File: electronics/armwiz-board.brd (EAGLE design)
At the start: 140.2 x 91.5 mm, 89 parts, among them J1 MICRO-SDCARD-CONNECTOR-330006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, J2 CORTEX_DEBUGSMD, U1 STM32F10XRXT6, U4 MIC5219-3.3V, X1 FH12-12S-1S, Y3 32.768kHz

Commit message: Really close now.
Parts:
- removed TP2, TP3, TP4: TPB1,27, testpad:B1,27
- added J15: Cortex Debug, SparkFun-Connectors:SAMTECH_FTSH-105-01
- added J16: ST-Link v2, SparkFun-Connectors:2X10
- added J17, J18: (no value), SparkFun-Connectors:1X01NS-KIT
- added R23: 100R, resistor:R0402
- added R24: 10K, resistor:R0402
- J14: device SparkFun-Connectors:1X25 -> PaxInstruments-Connectors:CONNECTORS_2X3_SMT_POSTS_T400
- moved J14 70.4 mm to (87.6, 33.0), flipped to the bottom, turned to 270 degrees
- moved R21 58.3 mm to (87.2, 4.50), turned to 270 degrees
- moved SJ2 37.9 mm to (85.0, 2.50), flipped to the bottom
- moved C18 37.2 mm to (83.2, 41.8), turned to 90 degrees
- moved R20 36.6 mm to (83.2, 37.2), turned to 90 degrees
- moved R4 32.4 mm to (82.0, 37.2)
- moved R2 32.0 mm to (84.5, 37.2)
- moved R18 29.8 mm to (85.8, 37.2), turned to 90 degrees
- moved C3 27.5 mm to (87.0, 34.0)
- moved R28 23.4 mm to (88.2, 34.0), turned to 270 degrees
- moved J2 20.9 mm to (87.2, 42.5), turned to 180 degrees
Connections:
- new net AD_GND: J15.3, J15.5, J15.9, J16.10, J16.12, J16.14, J16.16, J16.18, J16.20, J16.4, J16.6, J16.8
- new net AD_NRST: J15.10, J16.15
- new net AD_SWDCLK: J15.4, J16.9
- new net AD_SWDIO: J15.2, J16.7
- new net AD_SWO: J15.6, J16.13
- new net AD_TDI: J15.8, J16.5
- new net AD_VCC: J15.1, J16.1
- new net N$12: J2.6, R23.2
- net 3.3V: now also J14.1, J18.1, R24.2
- net BOOT0: now also J17.1; no longer TP2.TP
- net GND: now also J14.3; no longer J2.7
- net NRST: now also J14.5
- net SWDCLK: now also J14.2
- net SWDIO: now also J14.4
- net SWO: now also J14.6, R23.1, R24.1; no longer J2.6
- net USART1_RX: no longer TP3.TP
- net USART1_TX: no longer TP4.TP
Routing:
- net NRST: track 51.7 -> 104.7 mm, vias 1 -> 4
- net SWO: track 38.6 -> 91.6 mm, vias 0 -> 1
- net SW_A: track 54.6 -> 105.6 mm, vias 1 -> 2
- net SW_B: track 54.2 -> 91.2 mm, vias 1 -> 2
- net SWDIO: track 66.3 -> 99.2 mm, vias 1 -> 3
- net SWDCLK: track 63.0 -> 95.0 mm, vias 1 -> 3
- net RTC_BAT: track 47.2 -> 70.0 mm
- net SW_C: track 60.2 -> 83.0 mm, vias 1 -> 2
- net BOOT0: track 51.5 -> 74.0 mm, vias 1 -> 2
- net GND: track 81.1 -> 98.2 mm, vias 33 -> 41
- net BOOT1: track 55.3 -> 71.1 mm, vias 1 -> 3
- net 3.3V: track 47.8 -> 59.8 mm, vias 20 -> 28
- net N$13: track 0.00 -> 3.16 mm, vias 0 -> 1
- net N$12: track 0.00 -> 2.50 mm, vias 0 -> 1
- net N$5: track 0.00 -> 2.28 mm, vias 0 -> 1
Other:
- board size 140.2 x 91.5 mm -> 140.2 x 92.3 mm

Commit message: Four more wires.
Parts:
- added J22: (no value), SparkFun-Connectors:1X01
- moved J15 0.75 mm to (66.8, 35.5)
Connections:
- net PC1: now also J22.1
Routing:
- net AD_GND: track 0.00 -> 41.5 mm
- net AD_TDI: track 0.00 -> 13.5 mm, vias 0 -> 1
- net AD_VCC: track 0.00 -> 12.6 mm
- net AD_SWO: track 0.00 -> 7.11 mm
- net GND: track 98.2 -> 104.0 mm, vias 41 -> 44
- net AD_NRST: track 0.00 -> 5.65 mm
- net AD_SWDIO: track 0.00 -> 4.59 mm
- net AD_SWDCLK: track 0.00 -> 4.07 mm
- net N$14: track 0.00 -> 3.81 mm, vias 0 -> 1
- net SW_A: track 105.6 -> 102.8 mm
- net NRST: track 104.7 -> 102.5 mm
- net 3.3V: track 59.8 -> 61.3 mm
- net SW_B: track 91.2 -> 89.8 mm

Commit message: Added datasheets. This might be the final board layout and routing. Waiting on feedback.
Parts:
- removed J32, J9: (no value), SparkFun-Connectors:1X01
- removed R28: 10K, resistor:R0402
- added C12, C16, C17: 10uF, resistor:C0402K
- added C5, C7: 0.1uF, resistor:C0402K
- added J$1: SMA_EDGE, SparkFun-Connectors:SMA-EDGE
- added J23: (no value), SparkFun-Connectors:1X01
- added J25: (no value), PaxInstruments-Connectors:CONNECTORS_2X3_SMT_POSTS_T400
- added R25, R26: 10K, resistor:R0402
- moved J26 84.6 mm to (29.2, 43.2)
- moved J27 84.6 mm to (26.7, 43.2)
- moved U$6 74.5 mm to (73.3, 3.73), flipped to the bottom
- moved J21 5.08 mm to (55.9, 18.4)
- moved J20 2.54 mm to (50.8, 18.4)
- moved J11 2.54 mm to (40.6, 18.4)
- moved J22 2.54 mm to (48.3, 18.4)
- moved J24 2.54 mm to (38.1, 18.4)
- moved J33 2.54 mm to (45.7, 18.4)
- moved J7 2.54 mm to (43.2, 18.4)
- moved J8 2.54 mm to (53.3, 18.4)
- moved U$7 1.68 mm to (34.5, 12.8)
- moved C8 0.25 mm to (31.0, 14.2), turned to 180 degrees
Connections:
- removed net PB11: J9.1, U1.30
- removed net PC5: J32.1, U1.25
- new net N$14: J$1.GND@1, J$1.GND@3, J26.1
- new net N$15: J$1.GND@0, J$1.GND@2, J23.1
- new net N$16: R25.1, U$3.P$1
- new net N$20: J$1.SIG, J27.1
- new net VBAT2: R25.2, R26.1, U1.25
- net 3.3V: now also C12.2, C16.2, C17.2, C5.1, C7.1, J25.1; no longer R28.2
- net GND: now also C12.1, C16.1, C17.1, C5.2, C7.2, J25.5, R26.2
- net NRST: no longer R28.1
- net USART1_RX: now also J25.2; no longer J26.1
- net USART1_TX: now also J25.4; no longer J27.1
- net VBUS: now also U1.30
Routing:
- net VBAT2: track 0.00 -> 67.7 mm, vias 0 -> 2
- net PC5: track 46.8 -> 0.00 mm, vias 2 -> 0
- net SW_D: track 8.68 -> 42.7 mm, vias 0 -> 2
- net PB11: track 29.7 -> 0.00 mm, vias 2 -> 0
- net SW_E: track 7.76 -> 33.1 mm, vias 0 -> 2
- net USART1_RX: track 60.3 -> 46.8 mm
- net VBUS: track 25.4 -> 36.6 mm
- net 3.3V: track 61.3 -> 71.5 mm, vias 28 -> 30
- net N$15: track 0.00 -> 10.2 mm
- net N$16: track 0.00 -> 10.2 mm, vias 0 -> 1
- net USART1_TX: track 57.5 -> 48.9 mm, vias 1 -> 3
- net PC13: track 39.7 -> 33.0 mm
- net N$14: track 3.81 -> 10.2 mm, vias 1 -> 0
- net N$20: track 0.00 -> 5.08 mm
- net GND: track 104.0 -> 109.0 mm, vias 44 -> 50
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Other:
- board size 140.2 x 92.3 mm -> 99.1 x 51.5 mm
- board text added: "Armwiz v0.1"
- board text removed: "T400 v0.14"
- board text removed: "paxinstruments.com/products/sku927"

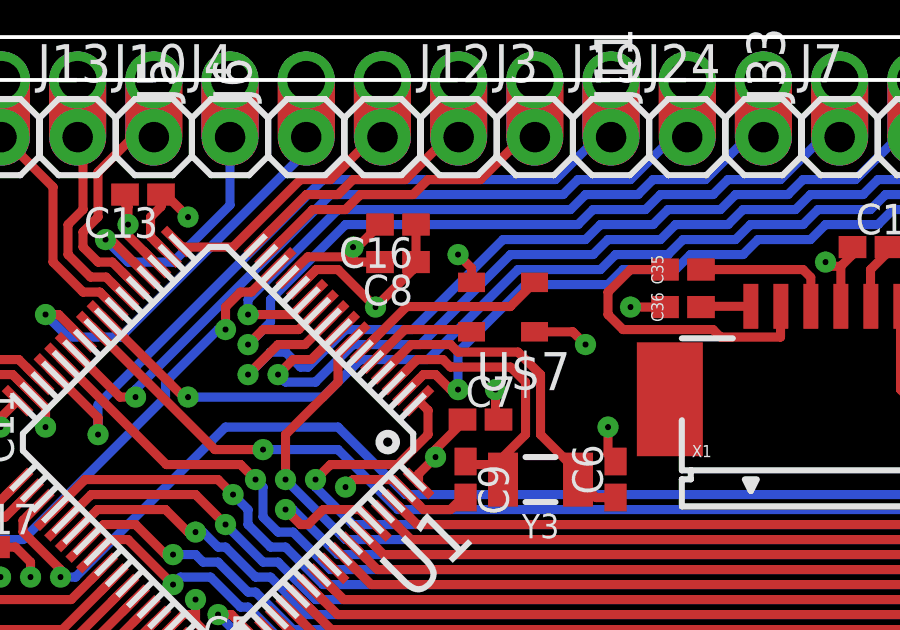
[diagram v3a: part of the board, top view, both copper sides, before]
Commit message: Fixed MEMS oscillator issue. Closes #3.
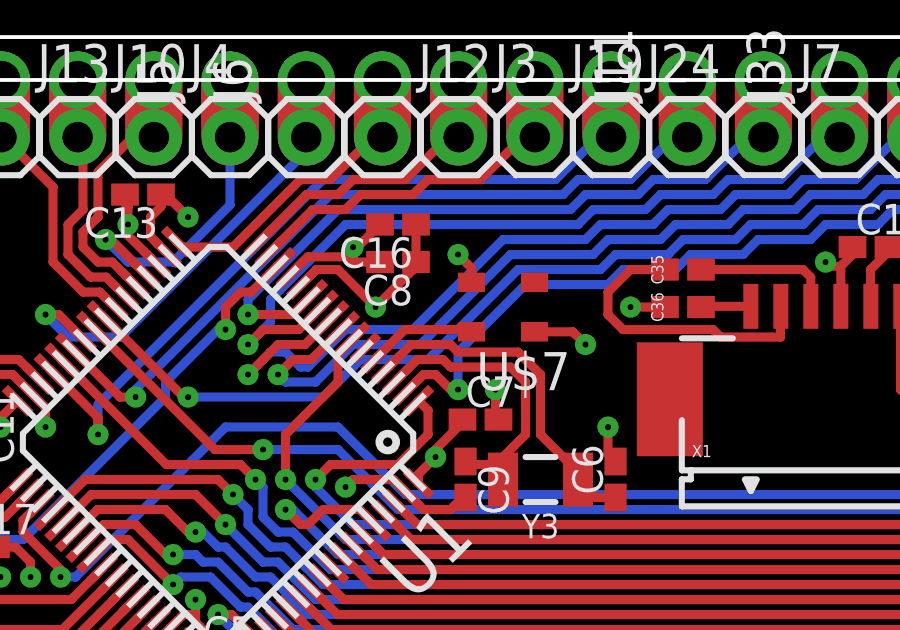
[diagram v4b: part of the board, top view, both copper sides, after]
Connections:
- removed net OSC_OUT: U$7.1, U1.6
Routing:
- net OSC_OUT: track 6.55 -> 0.00 mm
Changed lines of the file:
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@@
 <wire x1="29" y1="10.25" x2="29" y2="11.189340625" width="0.3048" layer="1"/>
-</signal>
-<signal name="OSC_OUT">
-<contactref element="U1" pad="6"/>
-<contactref element="U$7" pad="1"/>
-<wire x1="29.914390625" y1="11.396625" x2="31.267765625" y2="12.75" width="0.3048" layer="1"/>
-<wire x1="31.267765625" y1="12.75" x2="31.267765625" y2="12.767765625" width="0.3048" layer="1"/>
-<wire x1="31.267765625" y1="12.767765625" x2="34.742765625" y2="12.767765625" width="0.3048" layer="1"/>
-<wire x1="34.742765625" y1="12.767765625" x2="35.55" y2="13.575" width="0.3048" layer="1"/>
 </signal>
 <signal name="OSC_IN">

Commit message: Board passes ERC and DRC.
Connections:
- removed net N$17: J2.9
- net GND: now also J2.9
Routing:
- net GND: track 109.0 -> 110.2 mm, vias 50 -> 51
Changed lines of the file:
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@@
 </variantdefs>
 <classes>
-<class number="0" name="default" width="0.075" drill="0.2">
+<class number="0" name="Digital signal" width="0.075" drill="0.2">
 <clearance class="0" value="0.075"/>
 </class>
-<class number="1" name="power" width="0.075" drill="0.2">
+<class number="1" name="3.3V power" width="0.075" drill="0.2">
 <clearance class="1" value="0.075"/>
+</class>
+<class number="2" name="RTC battery" width="0.075" drill="0.2">
+<clearance class="2" value="0.075"/>
+</class>
+<class number="3" name="5V power" width="0.075" drill="0.2">
+<clearance class="3" value="0.075"/>
+</class>
+<class number="4" name="Analog signal" width="0.075" drill="0.2">
+<clearance class="4" value="0.075"/>
+</class>
+<class number="5" name="Ground" width="0.075" drill="0.2">
+<clearance class="5" value="0.075"/>
 </class>
 </classes>
@@
 <wire x1="79.92" y1="13.601" x2="79.92" y2="12.42" width="0.3048" layer="1"/>
 <wire x1="79.92" y1="12.42" x2="79.5" y2="12" width="0.3048" layer="1"/>
+<contactref element="J2" pad="9"/>
+<via x="89.75" y="43.75" extent="1-16" drill="0.2"/>
+<wire x1="89.79" y1="44.913" x2="89.75" y2="44.913" width="0.4064" layer="16"/>
+<wire x1="89.75" y1="44.913" x2="89.75" y2="43.75" width="0.4064" layer="16"/>
 </signal>
 <signal name="USB-">
@@
 <wire x1="9.627" y1="1.25" x2="11.1" y2="1.25" width="0.3048" layer="1"/>
 </signal>
-<signal name="RTC_BAT">
+<signal name="RTC_BAT" class="2">
 <contactref element="U1" pad="1"/>
 <contactref element="BAT1" pad="PWR@1"/>
@@
 <signal name="N$2">
 </signal>
-<signal name="N$17">
-<contactref element="J2" pad="9"/>
-</signal>
 <signal name="SWO">

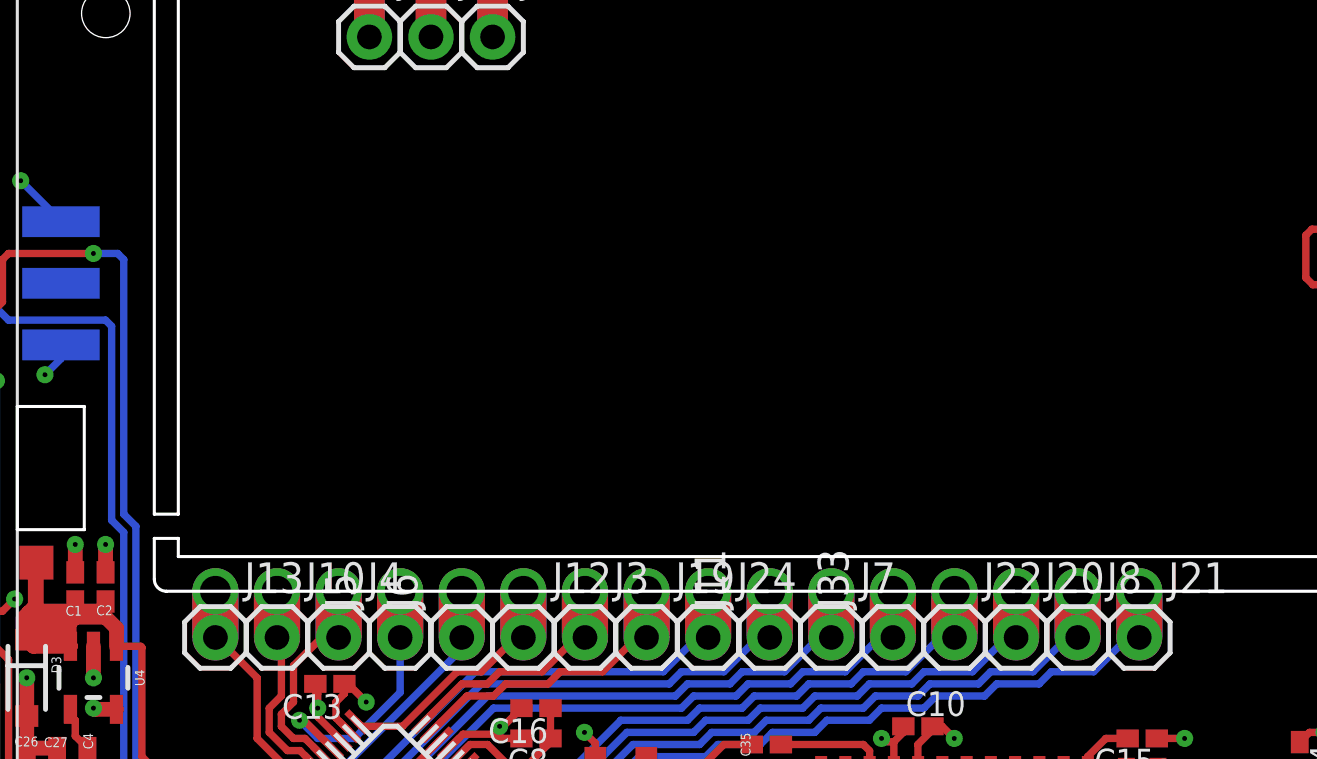
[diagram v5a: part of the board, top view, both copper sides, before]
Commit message: Added a Black Magic debugger to the prototyping area. This is not in the schematic and can be deleted.
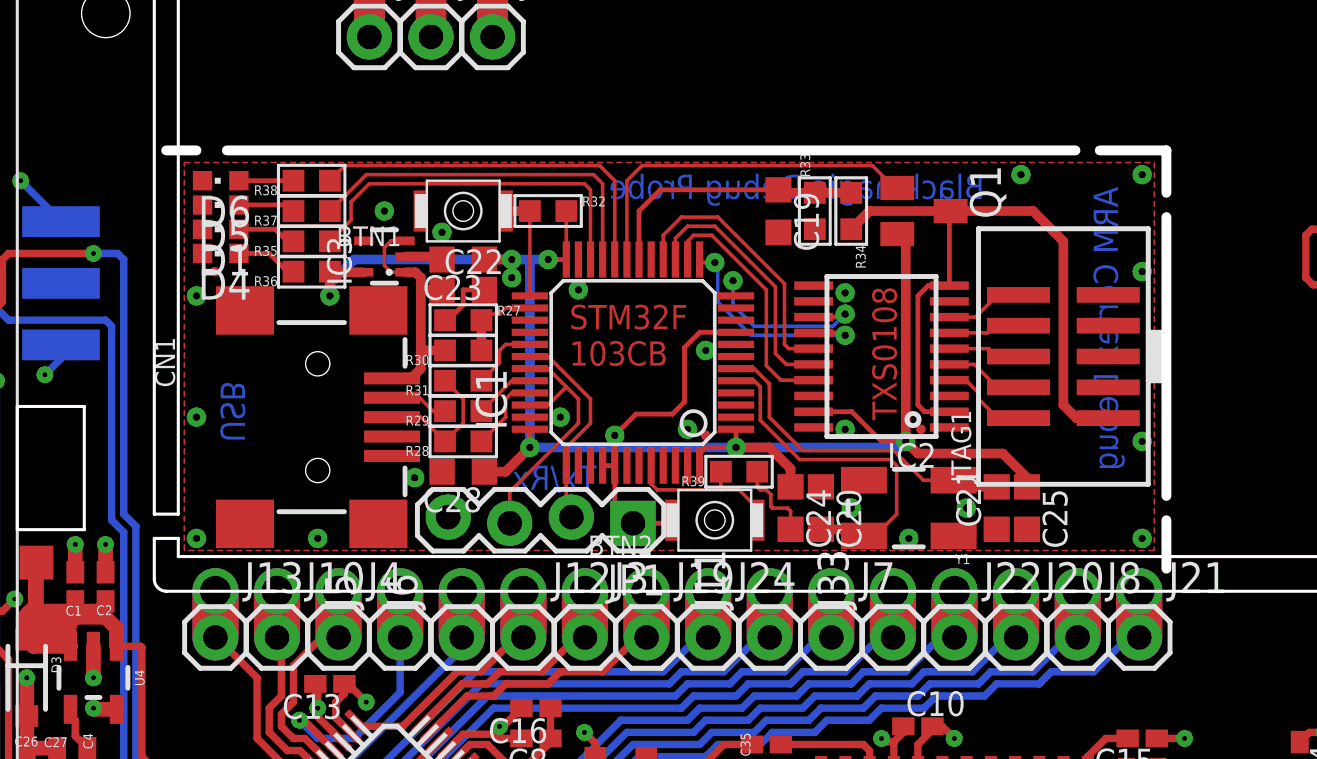
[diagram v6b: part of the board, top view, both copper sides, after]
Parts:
- added BTN1, BTN2: SPST.B3U-1000P(M)-B, omron:B3U-1000P(M)-B
- added C19, C24, C25, C28: 100nF, resistor:C0603K
- added C20, C21: 18pF, resistor:C0603K
- added C22, C23: 1µF, resistor:C0603K
- added CN1: (no value), microbuilder_v3:USB-MINIB
- added D1: RED, led:CHIPLED_0603
- added D4: GREEN, led:CHIPLED_0603
- added D5, D6: YELLOW, led:CHIPLED_0603
- added IC1: STM32F_48PIN, stm32f:TQFP48
- added IC2: TXS0108, dan-translate:TSSOP20
- added IC3: TLV70033DCK, tlv700:SC70-5L
- added JP1: (no value), SparkFun:1X04_LOCK
- added JTAG1: (no value), microbuilder_v3:2X05_1.27MM_SMT
- added Q1: IRLML5103, transistor-small-signal:SOT23
- added R27, R32, R33, R39: 10K, microbuilder:0603-MINI
- added R28, R29: 22Ω, microbuilder:0603-MINI
- added R30, R34: 4K7, microbuilder:0603-MINI
- added R31: 1K5, microbuilder:0603-MINI
- added R35, R36, R37, R38: 390Ω, microbuilder:0603-MINI
- added Y1: 8MHz, SparkFun:CRYSTAL-SMD-5X3
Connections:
- new net 3.3V1: BTN2.2, C23.1, C24.1, C25.1, C28.1, IC1.1, IC1.24, IC1.36, IC1.40, IC1.41, IC1.48, IC1.9, IC2.19, IC3.5, JP1.1, Q1.2, R32.2, R36.1
- new net 5.0V: C22.1, CN1.VBUS, IC3.1, IC3.3, R30.2
- new net BOOT2: BTN2.1, IC1.44, R39.2
- new net D+1: CN1.D+, R28.2, R31.2
- new net D-1: CN1.D-, R29.2
- new net FORCE_BOOTLOADER: BTN1.1, IC1.25, R32.1
- new net GND1: BTN1.2, C19.2, C20.1, C21.1, C22.2, C23.2, C24.2, C25.2, C28.2, CN1.GND, CN1.ID, D1.C, D4.C, D5.C, D6.C, IC1.23, IC1.35, IC1.47, IC1.8, IC2.11, IC2.12, IC2.18, IC2.20, IC3.2, JP1.4, JTAG1.3, JTAG1.5, JTAG1.9, R27.1, R33.1, R39.1
- new net LED0: IC1.20, R38.1
- new net LED1: IC1.21, R37.1
- new net LED2: IC1.22, R35.1
- new net LPC_XTAL2: C21.2, IC1.6, Y1.1
- new net N$10: D1.A, R35.2
- new net N$17: D4.A, R36.2
- new net N$25: D5.A, R37.2
- new net N$26: D6.A, R38.2
- new net OSC_IN1: C20.2, IC1.5, Y1.3
- new net PWR_BR: IC1.19, Q1.1
- new net RST: IC1.12, IC2.13
- new net RXD: IC1.31, IC1.34, JP1.3
- new net TARGET_POWER_ADC: C19.1, IC1.18, R33.2, R34.1
- new net TARGET_RST: IC2.8, JTAG1.10
- new net TARGET_TCK: IC2.5, JTAG1.4
- new net TARGET_TDI: IC2.7, JTAG1.8
- new net TARGET_TDO: IC2.6, JTAG1.6
- new net TARGET_TMS: IC2.4, JTAG1.2
- new net TCK: IC1.15, IC2.16
- new net TDI: IC1.13, IC2.14
- new net TDO: IC1.16, IC2.15
- new net TMS: IC1.14, IC2.17
- new net TPWR: IC2.10, IC2.2, JTAG1.1, Q1.3, R34.2
- new net TXD: IC1.30, IC1.37, JP1.2
- new net USB_DM: IC1.32, R29.1
- new net USB_DP: IC1.33, R28.1
- new net USB_ENUMERATE: IC1.29, R31.1
- new net VBUS1: IC1.26, R27.2, R30.1
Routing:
- net 3.3V1: track 0.00 -> 82.6 mm, vias 0 -> 7
- net TPWR: track 0.00 -> 28.9 mm
- net LED0: track 0.00 -> 15.5 mm
- net LED2: track 0.00 -> 15.2 mm
- net LED1: track 0.00 -> 15.2 mm
- net PWR_BR: track 0.00 -> 15.0 mm
- net OSC_IN1: track 0.00 -> 14.5 mm
- net LPC_XTAL2: track 0.00 -> 13.6 mm
- net TDO: track 0.00 -> 11.2 mm
- net TARGET_POWER_ADC: track 0.00 -> 11.2 mm
- net TCK: track 0.00 -> 10.8 mm
- net RXD: track 0.00 -> 10.6 mm
- net 5.0V: track 0.00 -> 10.4 mm
- net TMS: track 0.00 -> 10.4 mm
- net TDI: track 0.00 -> 9.51 mm, vias 0 -> 2
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- added copper zone on layer 1, net GND1
- added copper zone on layer 16, net GND1
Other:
- outline, holes or cut-outs redrawn
- board text added: "ARM Cortex Debug"
- board text added: "Blackmagic Debug Probe"
- board text added: "STM32F 103CB"
- board text added: "TXS0108"
- board text added: "Tx/Rx"
- board text added: "USB"
